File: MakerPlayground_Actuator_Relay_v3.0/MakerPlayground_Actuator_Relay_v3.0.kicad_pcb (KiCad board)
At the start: 2 copper layers, 45.5 x 32 mm, 12 parts, among them J1 Conn_01x04, J2 Terminal Block, J3 Terminal Block, K1 SANYOU_SRD_Form_C, Q1 Q_NPN_BEC

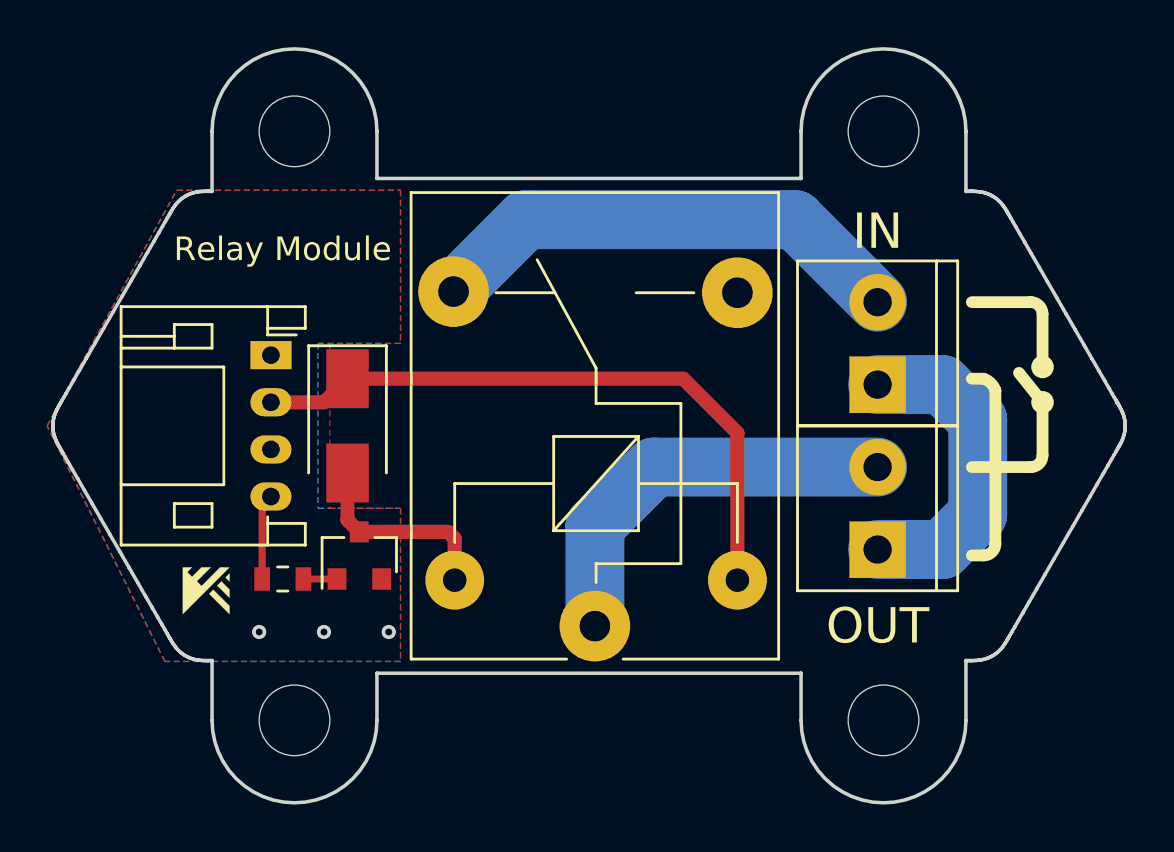
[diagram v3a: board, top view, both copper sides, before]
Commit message: Fix wiring error.
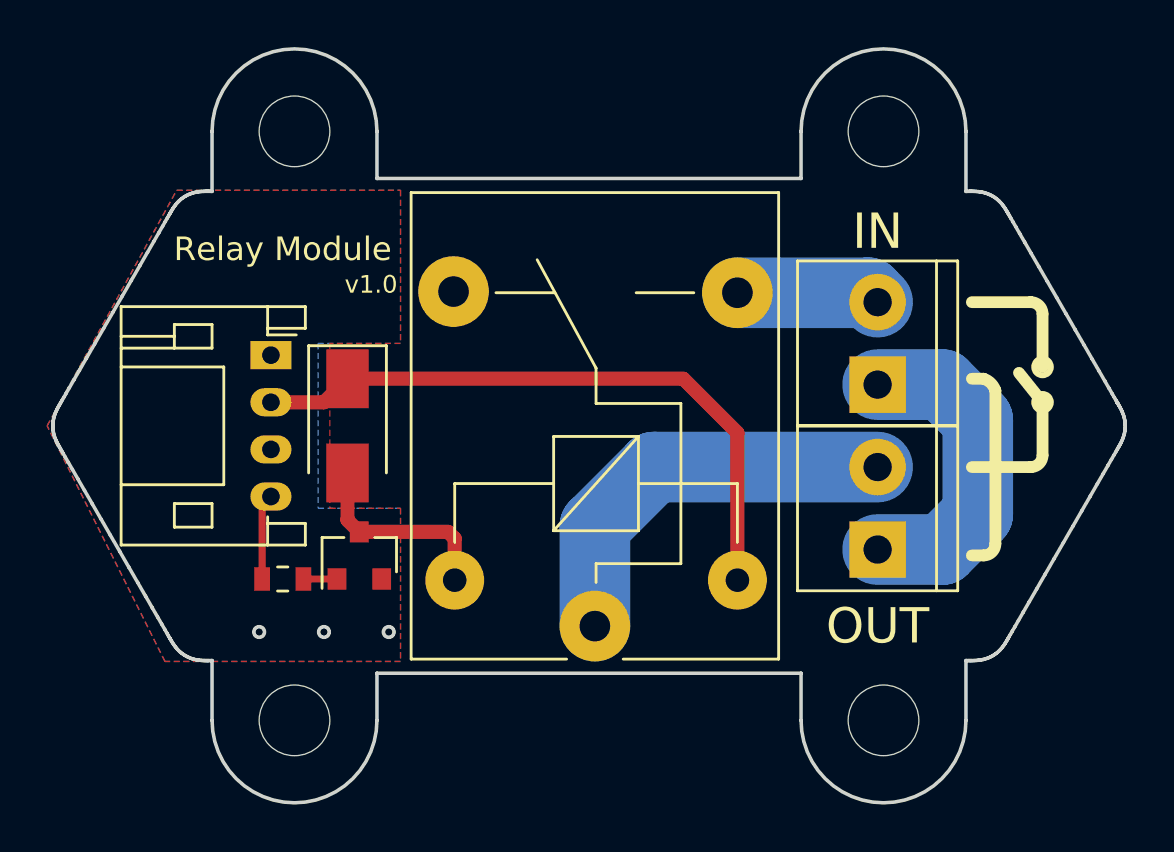
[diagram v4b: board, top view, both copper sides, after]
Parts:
- removed G***: LOGO, GiraffeTech-Utility:MakerPlayground_logo_2x2mm
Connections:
- K1 pad 3: Net-(K1-Pad3) -> Net-(J2-Pad2)
- K1 pad 4: Net-(J2-Pad2) -> Net-(K1-Pad4)
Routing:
- net Net-(J2-Pad2): track 20.7 -> 6.12 mm
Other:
- board text added: "v1.0"
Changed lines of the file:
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@@
   (general
     (thickness 1.6)
-    (drawings 316)
-    (tracks 27)
+    (drawings 315)
+    (tracks 26)
     (zones 0)
-    (modules 12)
+    (modules 11)
     (nets 11)
   )
@@
   (net 6 "Net-(J2-Pad2)")
   (net 7 "Net-(Q1-Pad1)")
-  (net 8 "Net-(K1-Pad3)")
-  (net 9 "Net-(J1-Pad3)")
-  (net 10 "Net-(J3-Pad2)")
+  (net 8 "Net-(J1-Pad3)")
+  (net 9 "Net-(J3-Pad2)")
+  (net 10 "Net-(K1-Pad4)")
   (net_class Default "This is the default net class."
     (clearance 0.2)
@@
     (add_net "Net-(J2-Pad2)")
     (add_net "Net-(J3-Pad2)")
-    (add_net "Net-(K1-Pad3)")
+    (add_net "Net-(K1-Pad4)")
     (add_net "Net-(Q1-Pad1)")
     (add_net SIG)
@@
       (net 1 VCC))
     (pad 3 thru_hole oval (at 4 0 270) (size 1.2 1.75) (drill 0.75) (layers *.Cu *.Mask)
-      (net 9 "Net-(J1-Pad3)"))
+      (net 8 "Net-(J1-Pad3)"))
     (pad 4 thru_hole oval (at 6 0 270) (size 1.2 1.75) (drill 0.75) (layers *.Cu *.Mask)
       (net 4 SIG))
@@
       (net 1 VCC))
     (pad 3 thru_hole circle (at 14.15 6.05 180) (size 3 3) (drill 1.3) (layers *.Cu *.Mask)
-      (net 8 "Net-(K1-Pad3)"))
+      (net 6 "Net-(J2-Pad2)"))
     (pad 4 thru_hole circle (at 14.2 -6 180) (size 3 3) (drill 1.3) (layers *.Cu *.Mask)
-      (net 6 "Net-(J2-Pad2)"))
+      (net 10 "Net-(K1-Pad4)"))
     (pad 5 thru_hole circle (at 1.95 -5.95 180) (size 2.5 2.5) (drill 1) (layers *.Cu *.Mask)
       (net 2 "Net-(D1-Pad2)"))
     (pad 1 thru_hole circle (at 0 0 180) (size 3 3) (drill 1.3) (layers *.Cu *.Mask)
-      (net 10 "Net-(J3-Pad2)"))
+      (net 9 "Net-(J3-Pad2)"))
     (model ${KISYS3DMOD}/Relay_THT.3dshapes/Relay_SPDT_SANYOU_SRD_Series_Form_C.wrl
       (at (xyz 0 0 0))
@@
       (net 5 "Net-(J2-Pad1)"))
     (pad 2 thru_hole circle (at 1.75 0 90) (size 2.4 2.4) (drill 1.2) (layers *.Cu *.Mask)
-      (net 10 "Net-(J3-Pad2)"))
+      (net 9 "Net-(J3-Pad2)"))
   )
   (module MountingHole:MountingHole_3mm locked (layer F.Cu)
@@
     (pad 1 np_thru_hole circle (at 0 0) (size 3 3) (drill 3) (layers *.Cu *.Mask))
   )
-  (module GiraffeTech-Utility:MakerPlayground_logo_2x2mm (layer F.Cu)
-    (at 127.25 107)
-    (fp_text reference G*** (at 0 0) (layer F.SilkS) hide
-      (effects (font (size 1.524 1.524) (thickness 0.3)))
-    )
-    (fp_text value LOGO (at 0.75 0) (layer F.SilkS) hide
-      (effects (font (size 1.524 1.524) (thickness 0.3)))
-    )
-    (fp_poly (pts (xy 0.992188 -0.564543) (xy 0.992164 -0.528929) (xy 0.992097 -0.495895) (xy 0.991991 -0.466261)
-      (xy 0.991852 -0.440843) (xy 0.991684 -0.420459) (xy 0.991492 -0.405926) (xy 0.991282 -0.398062)
-      (xy 0.99116 -0.396875) (xy 0.988207 -0.399571) (xy 0.980351 -0.407199) (xy 0.968291 -0.419067)
-      (xy 0.952725 -0.434484) (xy 0.934354 -0.452758) (xy 0.913876 -0.4732) (xy 0.906847 -0.480231)
-      (xy 0.823563 -0.563586) (xy 0.907875 -0.647899) (xy 0.992188 -0.732211) (xy 0.992188 -0.564543)) (layer F.SilkS) (width 0.01))
-    (fp_poly (pts (xy 0.992272 -0.049513) (xy 0.991238 0.124084) (xy 0.990203 0.297682) (xy 0.731231 0.038685)
-      (xy 0.472259 -0.220311) (xy 0.559597 -0.307581) (xy 0.646934 -0.394851) (xy 0.992272 -0.049513)) (layer F.SilkS) (width 0.01))
-    (fp_poly (pts (xy 0.306845 -0.036934) (xy 0.315366 -0.028902) (xy 0.328804 -0.015931) (xy 0.346812 0.001638)
-      (xy 0.369045 0.023463) (xy 0.39516 0.049204) (xy 0.424812 0.078521) (xy 0.457655 0.111071)
-      (xy 0.493344 0.146515) (xy 0.531535 0.184511) (xy 0.571883 0.224719) (xy 0.614044 0.266798)
-      (xy 0.649934 0.302669) (xy 0.992273 0.645025) (xy 0.990203 0.990203) (xy 0.559594 0.560703)
-      (xy 0.128984 0.131202) (xy 0.214278 0.045757) (xy 0.235683 0.024442) (xy 0.255382 0.005068)
-      (xy 0.272657 -0.011676) (xy 0.28679 -0.025103) (xy 0.297063 -0.034528) (xy 0.302757 -0.039261)
-      (xy 0.303583 -0.039687) (xy 0.306845 -0.036934)) (layer F.SilkS) (width 0.01))
-    (fp_poly (pts (xy 0.790777 -0.991434) (xy 0.988227 -0.990203) (xy -0.992187 0.990197) (xy -0.992187 -0.992187)
-      (xy -0.601395 -0.992187) (xy -0.646963 -0.945555) (xy -0.665935 -0.926151) (xy -0.688266 -0.903332)
-      (xy -0.711752 -0.879346) (xy -0.734194 -0.856442) (xy -0.745114 -0.845303) (xy -0.797697 -0.791685)
-      (xy -0.698482 -0.692529) (xy -0.599266 -0.593373) (xy -0.399829 -0.79278) (xy -0.200393 -0.992187)
-      (xy 0.195473 -0.992187) (xy -0.099139 -0.695955) (xy -0.39375 -0.399723) (xy -0.194618 -0.200591)
-      (xy 0.199355 -0.596628) (xy 0.593328 -0.992663) (xy 0.790777 -0.991434)) (layer F.SilkS) (width 0.01))
+  (gr_text IN (at 155.75 91.75) (layer F.SilkS)
+    (effects (font (size 1.5 1.5) (thickness 0.3)))
+  )
+  (gr_text v1.0 (at 134.25 94) (layer F.SilkS)
+    (effects (font (size 0.75 0.75) (thickness 0.15)))
   )
   (dimension 21 (width 0.3) (layer Dwgs.User)
@@
     (arrow2b (pts (xy 131 81.452681) (xy 132.126504 80.86626)))
   )
-  (gr_line (start 156 79) (end 156 114.5) (layer Dwgs.User) (width 0.2))
-  (gr_line (start 131 81) (end 131 114.25) (layer Dwgs.User) (width 0.2))
   (gr_text OUT (at 155.75 108.5) (layer F.SilkS)
-    (effects (font (size 1.5 1.5) (thickness 0.3)))
-  )
-  (gr_text IN (at 155.75 91.75) (layer F.SilkS)
     (effects (font (size 1.5 1.5) (thickness 0.3)))
   )
@@
   (segment (start 129.625 103.375) (end 130 103) (width 0.3) (layer F.Cu) (net 4))
   (segment (start 129.625 106.5) (end 129.625 103.375) (width 0.3) (layer F.Cu) (net 4))
-  (segment (start 158.5 98.25) (end 155.75 98.25) (width 2.5) (layer B.Cu) (net 5))
-  (segment (start 160 103.75) (end 160 99.75) (width 2.5) (layer B.Cu) (net 5))
-  (segment (start 160 99.75) (end 158.5 98.25) (width 2.5) (layer B.Cu) (net 5))
-  (segment (start 155.75 105.25) (end 158.5 105.25) (width 2.5) (layer B.Cu) (net 5))
-  (segment (start 158.5 105.25) (end 160 103.75) (width 2.5) (layer B.Cu) (net 5))
-  (segment (start 137.75 94.3) (end 140.8 91.25) (width 2.5) (layer B.Cu) (net 6))
-  (segment (start 152.25 91.25) (end 155.75 94.75) (width 2.5) (layer B.Cu) (net 6))
-  (segment (start 140.8 91.25) (end 152.25 91.25) (width 2.5) (layer B.Cu) (net 6))
+  (segment (start 158.5 98.25) (end 155.75 98.25) (width 3) (layer B.Cu) (net 5))
+  (segment (start 160 103.75) (end 160 99.75) (width 3) (layer B.Cu) (net 5))
+  (segment (start 160 99.75) (end 158.5 98.25) (width 3) (layer B.Cu) (net 5))
+  (segment (start 155.75 105.25) (end 158.5 105.25) (width 3) (layer B.Cu) (net 5))
+  (segment (start 158.5 105.25) (end 160 103.75) (width 3) (layer B.Cu) (net 5))
+  (segment (start 155.35 94.35) (end 155.75 94.75) (width 3) (layer B.Cu) (net 6))
+  (segment (start 149.8 94.35) (end 155.35 94.35) (width 3) (layer B.Cu) (net 6))
   (segment (start 131.375 106.5) (end 132.8 106.5) (width 0.3) (layer F.Cu) (net 7))
-  (segment (start 143.75 108.5) (end 143.75 104.25) (width 2.5) (layer B.Cu) (net 10))
-  (segment (start 146.25 101.75) (end 155.75 101.75) (width 2.5) (layer B.Cu) (net 10))
-  (segment (start 143.75 104.25) (end 146.25 101.75) (width 2.5) (layer B.Cu) (net 10))
+  (segment (start 143.75 108.5) (end 143.75 104.25) (width 3) (layer B.Cu) (net 9))
+  (segment (start 146.25 101.75) (end 155.75 101.75) (width 3) (layer B.Cu) (net 9))
+  (segment (start 143.75 104.25) (end 146.25 101.75) (width 3) (layer B.Cu) (net 9))
   (zone (net 3) (net_name GND) (layer F.Cu) (hatch edge 0.508)
     (connect_pads (clearance 0.3))

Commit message: Design complete.
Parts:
- moved J2 1.03 mm to (155.5, 95.5)
- moved J3 1.03 mm to (155.5, 104.5)
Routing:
- net Net-(J2-Pad1): track 13.7 -> 17.5 mm
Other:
- board text removed: "IN"
- board text removed: "OUT"
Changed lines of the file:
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@@
   (general
     (thickness 1.6)
-    (drawings 315)
+    (drawings 322)
     (tracks 26)
     (zones 0)
@@
   (page A4)
   (layers
-    (0 F.Cu signal)
-    (31 B.Cu signal)
+    (0 F.Cu signal hide)
+    (31 B.Cu signal hide)
     (32 B.Adhes user)
     (33 F.Adhes user)
@@
   )
   (module GiraffeTech-Connector:TerminalBlock_Dinkle_ED350V_1x02_P3.50mm_Horizontal (layer F.Cu)
-    (at 155.75 96.5 90)
+    (at 155.5 95.5 90)
     (fp_text reference J2 (at 0 5 90) (layer F.SilkS) hide
       (effects (font (size 1 1) (thickness 0.15)))
@@
   )
   (module GiraffeTech-Connector:TerminalBlock_Dinkle_ED350V_1x02_P3.50mm_Horizontal (layer F.Cu)
-    (at 155.75 103.5 90)
+    (at 155.5 104.5 90)
     (fp_text reference J3 (at 0 5 90) (layer F.SilkS) hide
       (effects (font (size 1 1) (thickness 0.15)))
@@
     (pad 1 np_thru_hole circle (at 0 0) (size 3 3) (drill 3) (layers *.Cu *.Mask))
   )
-  (gr_text IN (at 155.75 91.75) (layer F.SilkS)
-    (effects (font (size 1.5 1.5) (thickness 0.3)))
-  )
+  (gr_line (start 158.25 100.25) (end 158.75 99.75) (layer F.SilkS) (width 0.2))
+  (gr_line (start 157.75 99.75) (end 158.25 100.25) (layer F.SilkS) (width 0.2))
+  (gr_line (start 157.25 100.25) (end 157.75 99.75) (layer F.SilkS) (width 0.2))
+  (gr_line (start 156.75 99.75) (end 157.25 100.25) (layer F.SilkS) (width 0.2))
+  (gr_line (start 156.25 100.25) (end 156.75 99.75) (layer F.SilkS) (width 0.2))
+  (gr_line (start 155.75 99.75) (end 156.25 100.25) (layer F.SilkS) (width 0.2))
+  (gr_line (start 155.25 100.25) (end 155.75 99.75) (layer F.SilkS) (width 0.2))
+  (gr_line (start 154.75 99.75) (end 155.25 100.25) (layer F.SilkS) (width 0.2))
+  (gr_line (start 154.25 100.25) (end 154.75 99.75) (layer F.SilkS) (width 0.2))
+  (gr_line (start 153.75 99.75) (end 154.25 100.25) (layer F.SilkS) (width 0.2))
+  (gr_line (start 153.25 100.25) (end 153.75 99.75) (layer F.SilkS) (width 0.2))
+  (gr_line (start 152.75 99.75) (end 153.25 100.25) (layer F.SilkS) (width 0.2))
+  (gr_line (start 152.25 100.25) (end 152.75 99.75) (layer F.SilkS) (width 0.2))
   (gr_text v1.0 (at 134.25 94) (layer F.SilkS)
     (effects (font (size 0.75 0.75) (thickness 0.15)))
   )
-  (dimension 21 (width 0.3) (layer Dwgs.User)
-    (gr_text "21.000 mm" (at 175.85 100 90) (layer Dwgs.User)
-      (effects (font (size 1.5 1.5) (thickness 0.3)))
-    )
-    (feature1 (pts (xy 152.5 89.5) (xy 174.336421 89.5)))
-    (feature2 (pts (xy 152.5 110.5) (xy 174.336421 110.5)))
-    (crossbar (pts (xy 173.75 110.5) (xy 173.75 89.5)))
-    (arrow1a (pts (xy 173.75 89.5) (xy 174.336421 90.626504)))
-    (arrow1b (pts (xy 173.75 89.5) (xy 173.163579 90.626504)))
-    (arrow2a (pts (xy 173.75 110.5) (xy 174.336421 109.373496)))
-    (arrow2b (pts (xy 173.75 110.5) (xy 173.163579 109.373496)))
-  )
-  (dimension 20 (width 0.3) (layer Dwgs.User)
-    (gr_text "20.000 mm" (at 170.6 100 90) (layer Dwgs.User)
-      (effects (font (size 1.5 1.5) (thickness 0.3)))
-    )
-    (feature1 (pts (xy 159.5 90) (xy 169.086421 90)))
-    (feature2 (pts (xy 159.5 110) (xy 169.086421 110)))
-    (crossbar (pts (xy 168.5 110) (xy 168.5 90)))
-    (arrow1a (pts (xy 168.5 90) (xy 169.086421 91.126504)))
-    (arrow1b (pts (xy 168.5 90) (xy 167.913579 91.126504)))
-    (arrow2a (pts (xy 168.5 110) (xy 169.086421 108.873496)))
-    (arrow2b (pts (xy 168.5 110) (xy 167.913579 108.873496)))
-  )
-  (gr_line (start 162.75 99) (end 161.75 97.75) (layer F.SilkS) (width 0.5))
-  (gr_arc (start 162.25 95.25) (end 162.75 95.25) (angle -90) (layer F.SilkS) (width 0.5))
-  (gr_arc (start 162.25 101.25) (end 162.25 101.75) (angle -90) (layer F.SilkS) (width 0.5))
-  (gr_circle (center 162.75 97.5) (end 163.103553 97.5) (layer F.SilkS) (width 0.25))
-  (gr_circle (center 162.75 99) (end 163.103553 99) (layer F.SilkS) (width 0.25))
-  (gr_line (start 162.75 97.5) (end 162.75 95.25) (layer F.SilkS) (width 0.5))
-  (gr_line (start 162.75 101.25) (end 162.75 99) (layer F.SilkS) (width 0.5))
-  (gr_line (start 159.75 94.75) (end 162.25 94.75) (layer F.SilkS) (width 0.5))
-  (gr_line (start 159.75 101.75) (end 162.25 101.75) (layer F.SilkS) (width 0.5))
-  (gr_arc (start 160.25 105) (end 160.25 105.5) (angle -90) (layer F.SilkS) (width 0.5))
-  (gr_arc (start 160 98.75) (end 160.749999 98.500001) (angle -53.1) (layer F.SilkS) (width 0.5))
-  (gr_line (start 160.25 98) (end 159.75 98) (layer F.SilkS) (width 0.5))
-  (gr_line (start 160.75 105) (end 160.75 98.5) (layer F.SilkS) (width 0.5))
-  (gr_line (start 159.75 105.5) (end 160.25 105.5) (layer F.SilkS) (width 0.5))
+  (gr_line (start 162.4 100.75) (end 161.4 99.5) (layer F.SilkS) (width 0.5))
+  (gr_arc (start 161.9 94.25) (end 162.4 94.25) (angle -90) (layer F.SilkS) (width 0.5))
+  (gr_arc (start 161.9 102.25) (end 161.9 102.75) (angle -90) (layer F.SilkS) (width 0.5))
+  (gr_circle (center 162.4 99.25) (end 162.753553 99.25) (layer F.SilkS) (width 0.25))
+  (gr_circle (center 162.4 100.75) (end 162.753553 100.75) (layer F.SilkS) (width 0.25))
+  (gr_line (start 162.4 99.25) (end 162.4 94.25) (layer F.SilkS) (width 0.5))
+  (gr_line (start 162.4 102.25) (end 162.4 100.75) (layer F.SilkS) (width 0.5))
+  (gr_line (start 159.4 93.75) (end 161.9 93.75) (layer F.SilkS) (width 0.5))
+  (gr_line (start 159.4 102.75) (end 161.9 102.75) (layer F.SilkS) (width 0.5))
+  (gr_arc (start 159.9 106) (end 159.9 106.5) (angle -90) (layer F.SilkS) (width 0.5))
+  (gr_arc (start 159.65 97.75) (end 160.399999 97.500001) (angle -53.1) (layer F.SilkS) (width 0.5))
+  (gr_line (start 159.9 97) (end 159.4 97) (layer F.SilkS) (width 0.5))
+  (gr_line (start 160.4 106) (end 160.4 97.5) (layer F.SilkS) (width 0.5))
+  (gr_line (start 159.4 106.5) (end 159.9 106.5) (layer F.SilkS) (width 0.5))
   (gr_line (start 159.5 112.5) (end 159.5 109.96) (layer Edge.Cuts) (width 0.15))
   (gr_line (start 152.5 112.5) (end 152.5 110.5) (layer Edge.Cuts) (width 0.15))
@@
   (gr_line (start 134.5 87.5) (end 134.5 89.5) (layer Edge.Cuts) (width 0.15))
   (gr_arc (start 131 87.5) (end 134.5 87.5) (angle -180) (layer Edge.Cuts) (width 0.15))
-  (dimension 25 (width 0.3) (layer Dwgs.User)
-    (gr_text "25.000 mm" (at 119.9 100 90) (layer Dwgs.User)
-      (effects (font (size 1.5 1.5) (thickness 0.3)))
-    )
-    (feature1 (pts (xy 128.5 87.5) (xy 121.413579 87.5)))
-    (feature2 (pts (xy 128.5 112.5) (xy 121.413579 112.5)))
-    (crossbar (pts (xy 122 112.5) (xy 122 87.5)))
-    (arrow1a (pts (xy 122 87.5) (xy 122.586421 88.626504)))
-    (arrow1b (pts (xy 122 87.5) (xy 121.413579 88.626504)))
-    (arrow2a (pts (xy 122 112.5) (xy 122.586421 111.373496)))
-    (arrow2b (pts (xy 122 112.5) (xy 121.413579 111.373496)))
-  )
-  (dimension 25 (width 0.3) (layer Dwgs.User)
-    (gr_text "25.000 mm" (at 143.5 79.352681) (layer Dwgs.User)
-      (effects (font (size 1.5 1.5) (thickness 0.3)))
-    )
-    (feature1 (pts (xy 156 86.75) (xy 156 80.86626)))
-    (feature2 (pts (xy 131 86.75) (xy 131 80.86626)))
-    (crossbar (pts (xy 131 81.452681) (xy 156 81.452681)))
-    (arrow1a (pts (xy 156 81.452681) (xy 154.873496 82.039102)))
-    (arrow1b (pts (xy 156 81.452681) (xy 154.873496 80.86626)))
-    (arrow2a (pts (xy 131 81.452681) (xy 132.126504 82.039102)))
-    (arrow2b (pts (xy 131 81.452681) (xy 132.126504 80.86626)))
-  )
-  (gr_text OUT (at 155.75 108.5) (layer F.SilkS)
-    (effects (font (size 1.5 1.5) (thickness 0.3)))
-  )
   (gr_line (start 160.2551 90.097881) (end 160.175297 90.080642) (layer Edge.Cuts) (width 0.15))
   (gr_line (start 159.878935 90.048017) (end 159.816556 90.045969) (layer Edge.Cuts) (width 0.15))
@@
   (segment (start 129.625 103.375) (end 130 103) (width 0.3) (layer F.Cu) (net 4))
   (segment (start 129.625 106.5) (end 129.625 103.375) (width 0.3) (layer F.Cu) (net 4))
-  (segment (start 158.5 98.25) (end 155.75 98.25) (width 3) (layer B.Cu) (net 5))
-  (segment (start 160 103.75) (end 160 99.75) (width 3) (layer B.Cu) (net 5))
-  (segment (start 160 99.75) (end 158.5 98.25) (width 3) (layer B.Cu) (net 5))
-  (segment (start 155.75 105.25) (end 158.5 105.25) (width 3) (layer B.Cu) (net 5))
-  (segment (start 158.5 105.25) (end 160 103.75) (width 3) (layer B.Cu) (net 5))
-  (segment (start 155.35 94.35) (end 155.75 94.75) (width 3) (layer B.Cu) (net 6))
-  (segment (start 149.8 94.35) (end 155.35 94.35) (width 3) (layer B.Cu) (net 6))
+  (segment (start 155.5 106.25) (end 159.25 106.25) (width 3) (layer B.Cu) (net 5))
+  (segment (start 159.25 106.25) (end 160.5 105) (width 3) (layer B.Cu) (net 5))
+  (segment (start 160.5 105) (end 160.5 98.5) (width 3) (layer B.Cu) (net 5))
+  (segment (start 159.25 97.25) (end 155.5 97.25) (width 3) (layer B.Cu) (net 5))
+  (segment (start 160.5 98.5) (end 159.25 97.25) (width 3) (layer B.Cu) (net 5))
+  (segment (start 150.4 93.75) (end 149.8 94.35) (width 3) (layer B.Cu) (net 6))
+  (segment (start 155.5 93.75) (end 150.4 93.75) (width 3) (layer B.Cu) (net 6))
   (segment (start 131.375 106.5) (end 132.8 106.5) (width 0.3) (layer F.Cu) (net 7))
-  (segment (start 143.75 108.5) (end 143.75 104.25) (width 3) (layer B.Cu) (net 9))
-  (segment (start 146.25 101.75) (end 155.75 101.75) (width 3) (layer B.Cu) (net 9))
-  (segment (start 143.75 104.25) (end 146.25 101.75) (width 3) (layer B.Cu) (net 9))
+  (segment (start 143.75 108.5) (end 143.75 103.75) (width 3) (layer B.Cu) (net 9))
+  (segment (start 144.75 102.75) (end 155.5 102.75) (width 3) (layer B.Cu) (net 9))
+  (segment (start 143.75 103.75) (end 144.75 102.75) (width 3) (layer B.Cu) (net 9))
   (zone (net 3) (net_name GND) (layer F.Cu) (hatch edge 0.508)
     (connect_pads (clearance 0.3))
